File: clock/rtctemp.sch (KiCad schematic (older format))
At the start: 15 parts, among them U601 ADT7410, U602 DS3231, U603 ADT7410

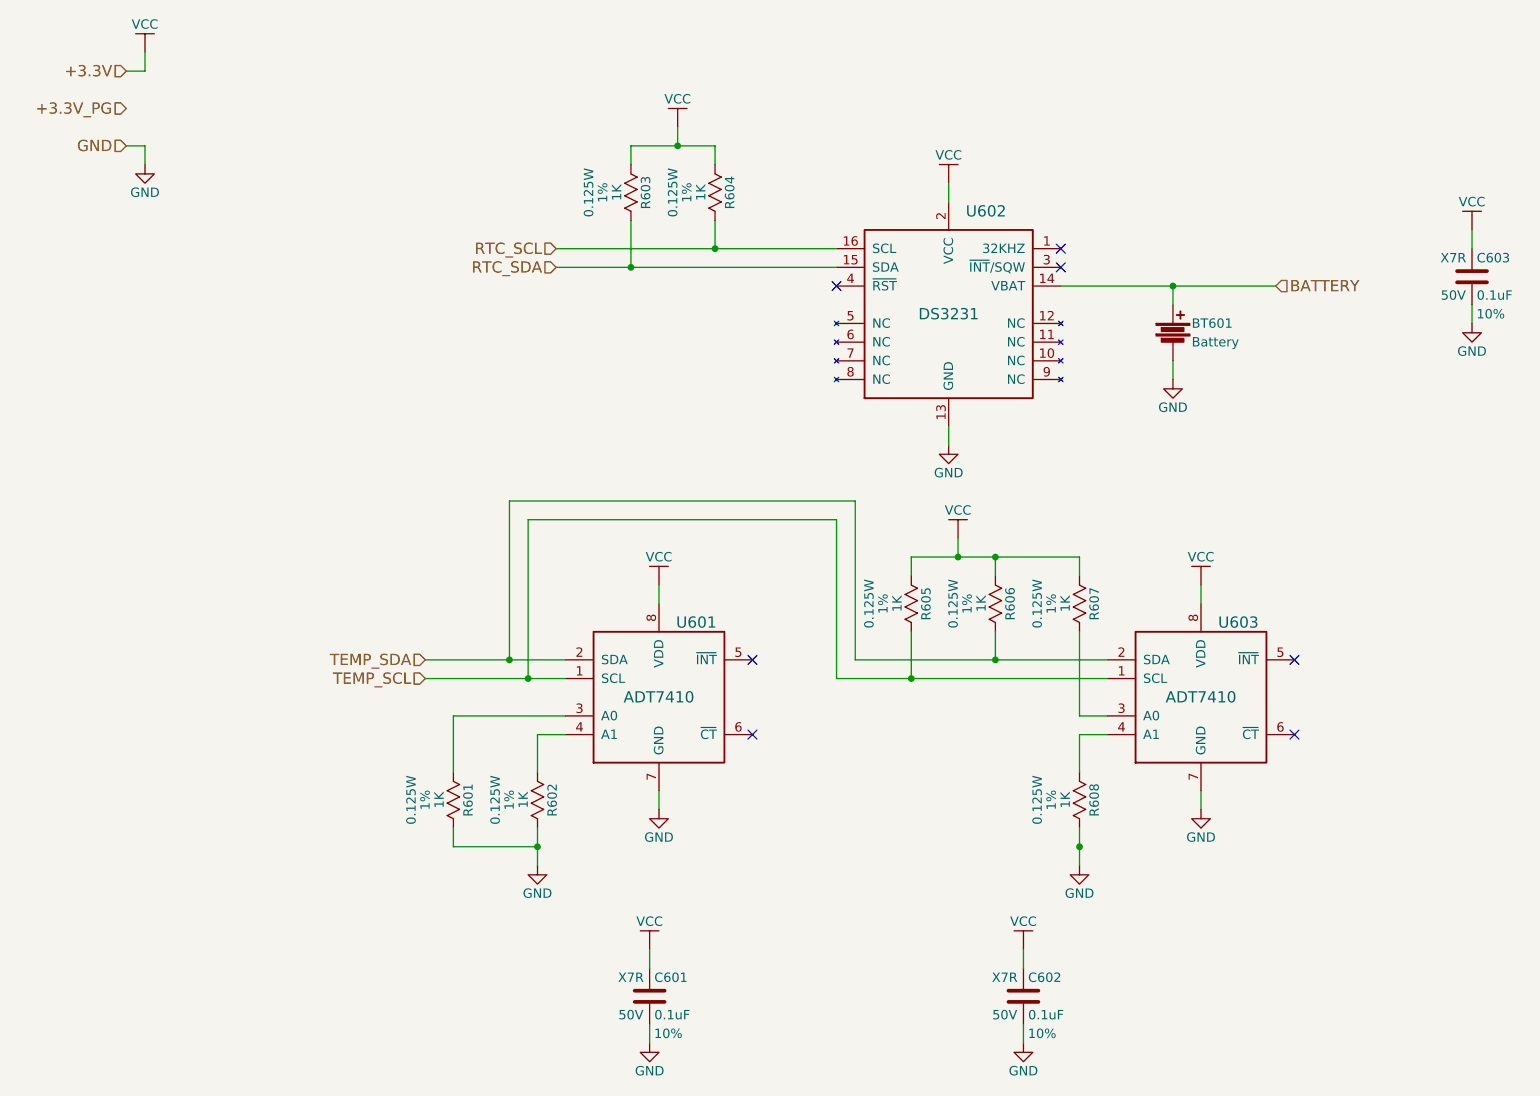
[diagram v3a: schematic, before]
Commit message: Make component parameters consistent for BOM.
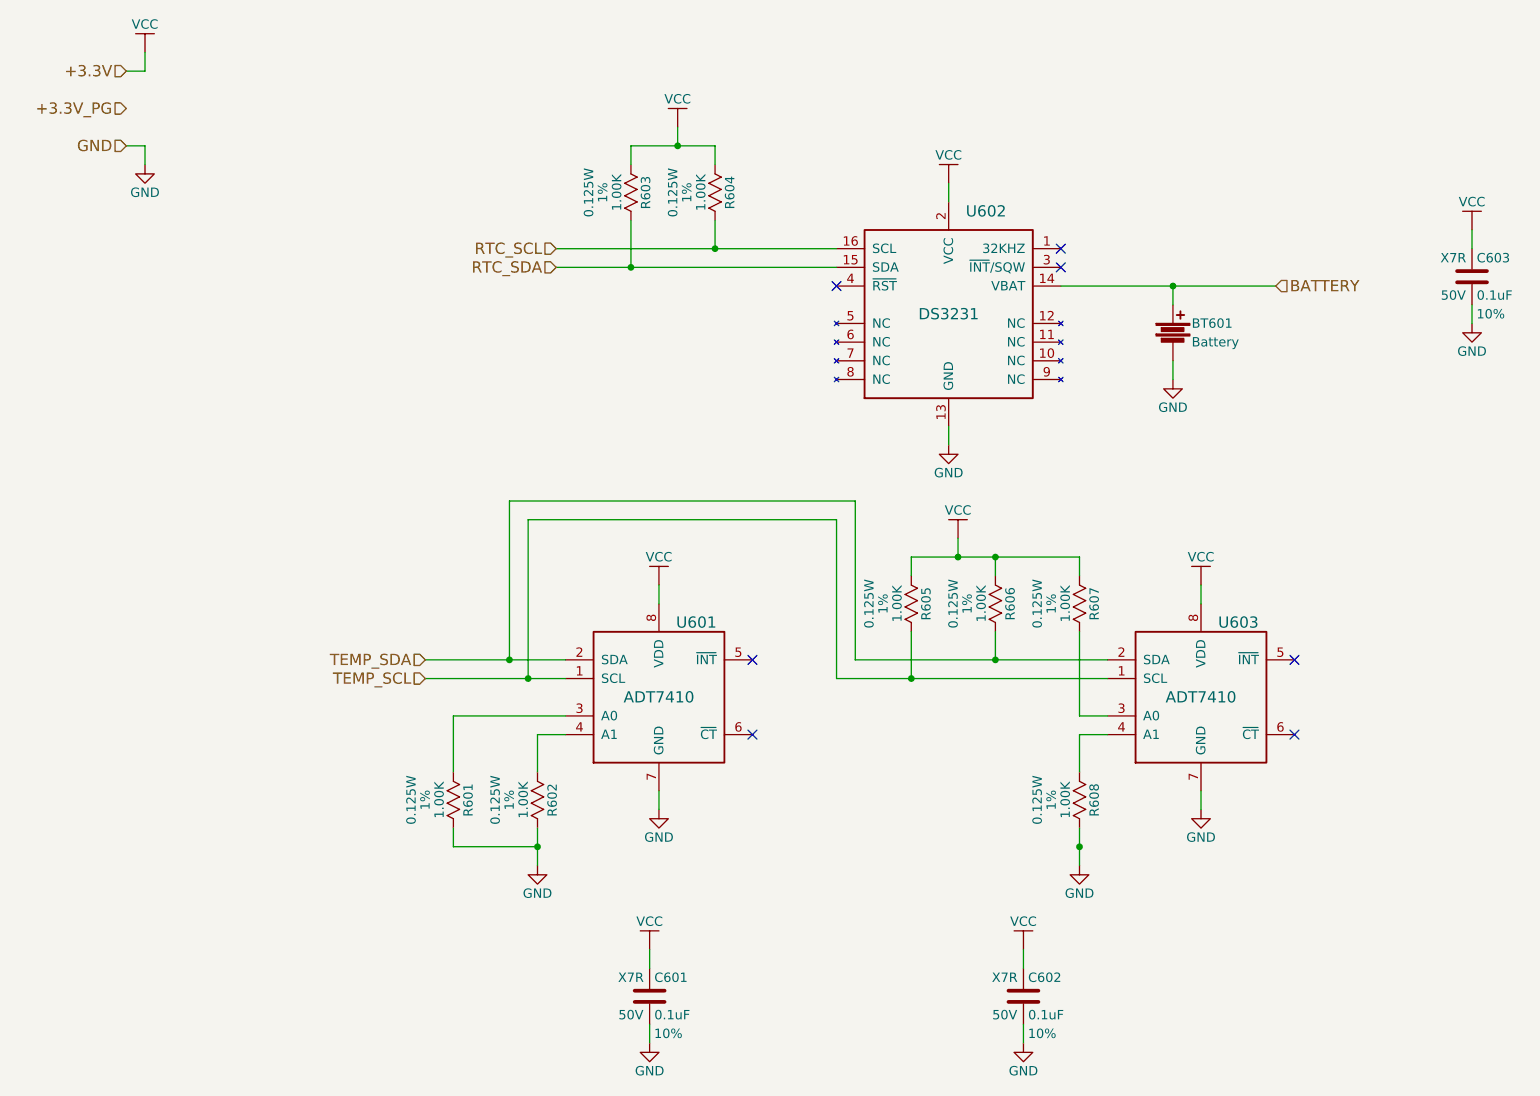
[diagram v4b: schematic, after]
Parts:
- R601, R602, R603, R604, R605, R606, R607, R608: value 1K -> 1.00K
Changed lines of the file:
@@
 P 4050 2050
 F 0 "R603" V 4130 2050 50  0000 C CNN
-F 1 "1K" V 3975 2050 50  0000 C CNN
+F 1 "1.00K" V 3975 2050 50  0000 C CNN
 F 2 "Resistors_SMD:R_0805_HandSoldering" V 3980 2050 30  0001 C CNN
 F 3 "" V 4130 2050 30  0000 C CNN
@@
 P 4500 2050
 F 0 "R604" V 4580 2050 50  0000 C CNN
-F 1 "1K" V 4425 2050 50  0000 C CNN
+F 1 "1.00K" V 4425 2050 50  0000 C CNN
 F 2 "Resistors_SMD:R_0805_HandSoldering" V 4430 2050 30  0001 C CNN
 F 3 "" V 4580 2050 30  0000 C CNN
@@
 P 5550 4250
 F 0 "R605" V 5630 4250 50  0000 C CNN
-F 1 "1K" V 5475 4250 50  0000 C CNN
+F 1 "1.00K" V 5475 4250 50  0000 C CNN
 F 2 "Resistors_SMD:R_0805_HandSoldering" V 5480 4250 30  0001 C CNN
 F 3 "" V 5630 4250 30  0000 C CNN
@@
 P 6000 4250
 F 0 "R606" V 6080 4250 50  0000 C CNN
-F 1 "1K" V 5925 4250 50  0000 C CNN
+F 1 "1.00K" V 5925 4250 50  0000 C CNN
 F 2 "Resistors_SMD:R_0805_HandSoldering" V 5930 4250 30  0001 C CNN
 F 3 "" V 6080 4250 30  0000 C CNN
@@
 P 3100 5300
 F 0 "R601" V 3180 5300 50  0000 C CNN
-F 1 "1K" V 3025 5300 50  0000 C CNN
+F 1 "1.00K" V 3025 5300 50  0000 C CNN
 F 2 "Resistors_SMD:R_0805_HandSoldering" V 3030 5300 30  0001 C CNN
 F 3 "" V 3180 5300 30  0000 C CNN
@@
 P 3550 5300
 F 0 "R602" V 3630 5300 50  0000 C CNN
-F 1 "1K" V 3475 5300 50  0000 C CNN
+F 1 "1.00K" V 3475 5300 50  0000 C CNN
 F 2 "Resistors_SMD:R_0805_HandSoldering" V 3480 5300 30  0001 C CNN
 F 3 "" V 3630 5300 30  0000 C CNN
@@
 P 6450 5300
 F 0 "R608" V 6530 5300 50  0000 C CNN
-F 1 "1K" V 6375 5300 50  0000 C CNN
+F 1 "1.00K" V 6375 5300 50  0000 C CNN
 F 2 "Resistors_SMD:R_0805_HandSoldering" V 6380 5300 30  0001 C CNN
 F 3 "" V 6530 5300 30  0000 C CNN
@@
 P 6450 4250
 F 0 "R607" V 6530 4250 50  0000 C CNN
-F 1 "1K" V 6375 4250 50  0000 C CNN
+F 1 "1.00K" V 6375 4250 50  0000 C CNN
 F 2 "Resistors_SMD:R_0805_HandSoldering" V 6380 4250 30  0001 C CNN
 F 3 "" V 6530 4250 30  0000 C CNN

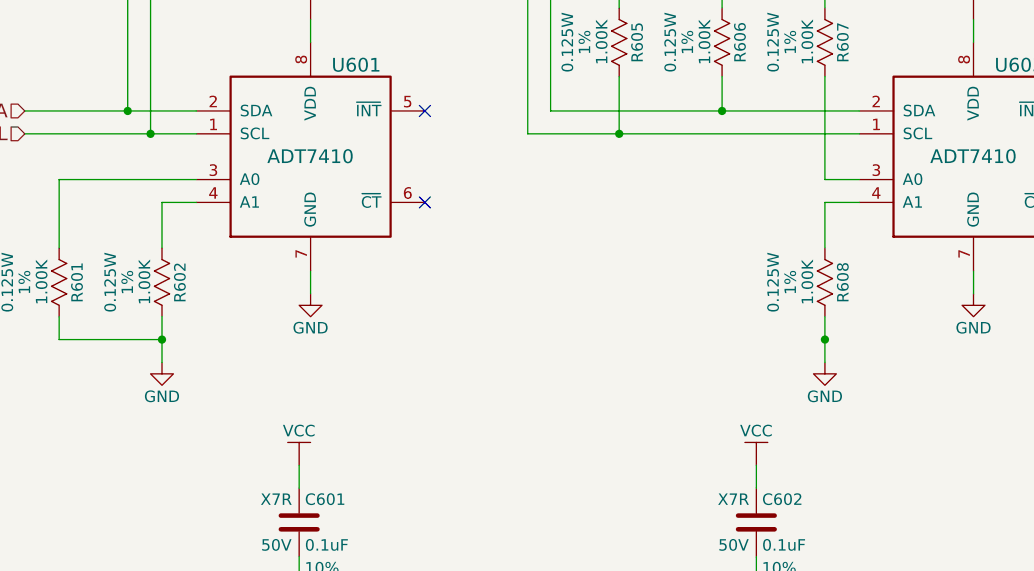
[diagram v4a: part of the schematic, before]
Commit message: Add net names to most of the nets.
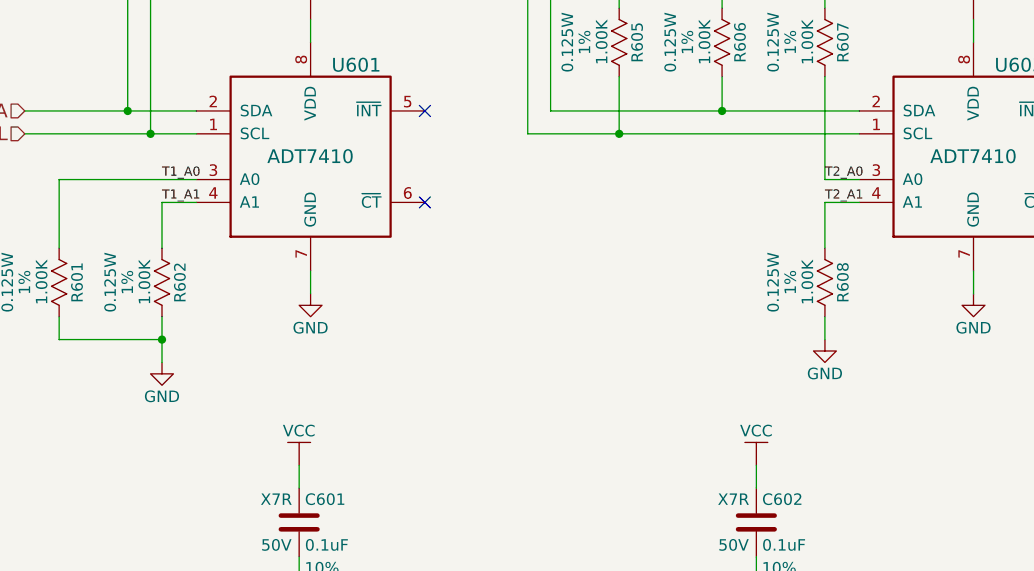
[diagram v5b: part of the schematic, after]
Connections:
- net T1_A0: now reaches R601.1, U601.3 (A0)
- net T1_A1: now reaches R602.1, U601.4 (A1)
- net T2_A0: now reaches R607.2, U603.3 (A0)
- net T2_A1: now reaches R608.1, U603.4 (A1)
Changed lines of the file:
@@
 RTC_SDA
 $Comp
-L GND #PWR076
+L GND #PWR078
 U 1 1 5636B600
 P 1450 1900
-F 0 "#PWR076" H 1450 1650 50  0001 C CNN
+F 0 "#PWR078" H 1450 1650 50  0001 C CNN
 F 1 "GND" H 1450 1750 50  0000 C CNN
 F 2 "" H 1450 1900 60  0000 C CNN
@@
 	5750 3400 5750 3300
 $Comp
-L GND #PWR077
+L GND #PWR079
 U 1 1 5636B6C4
 P 5750 3400
-F 0 "#PWR077" H 5750 3150 50  0001 C CNN
+F 0 "#PWR079" H 5750 3150 50  0001 C CNN
 F 1 "GND" H 5750 3250 50  0000 C CNN
 F 2 "" H 5750 3400 60  0000 C CNN
@@
 $EndComp
 $Comp
-L VCC #PWR078
+L VCC #PWR080
 U 1 1 5636B791
 P 1450 1300
-F 0 "#PWR078" H 1450 1150 50  0001 C CNN
+F 0 "#PWR080" H 1450 1150 50  0001 C CNN
 F 1 "VCC" H 1450 1450 50  0000 C CNN
 F 2 "" H 1450 1300 60  0000 C CNN
@@
 	1450 1400 1450 1300
 $Comp
-L VCC #PWR079
+L VCC #PWR081
 U 1 1 5636B7D2
 P 5750 2000
-F 0 "#PWR079" H 5750 1850 50  0001 C CNN
+F 0 "#PWR081" H 5750 1850 50  0001 C CNN
 F 1 "VCC" H 5750 2150 50  0000 C CNN
 F 2 "" H 5750 2000 60  0000 C CNN
@@
 	4500 1800 4500 1900
 $Comp
-L VCC #PWR080
+L VCC #PWR082
 U 1 1 5636BBAE
 P 4300 1700
-F 0 "#PWR080" H 4300 1550 50  0001 C CNN
+F 0 "#PWR082" H 4300 1550 50  0001 C CNN
 F 1 "VCC" H 4300 1850 50  0000 C CNN
 F 2 "" H 4300 1700 60  0000 C CNN
@@
 	6950 2550 6950 2650
 $Comp
-L GND #PWR081
+L GND #PWR083
 U 1 1 5636BC94
 P 6950 3050
-F 0 "#PWR081" H 6950 2800 50  0001 C CNN
+F 0 "#PWR083" H 6950 2800 50  0001 C CNN
 F 1 "GND" H 6950 2900 50  0000 C CNN
 F 2 "" H 6950 3050 60  0000 C CNN
@@
 $EndComp
 $Comp
-L VCC #PWR082
+L VCC #PWR084
 U 1 1 5636C0D5
 P 4200 4150
-F 0 "#PWR082" H 4200 4000 50  0001 C CNN
+F 0 "#PWR084" H 4200 4000 50  0001 C CNN
 F 1 "VCC" H 4200 4300 50  0000 C CNN
 F 2 "" H 4200 4150 60  0000 C CNN
@@
 	7100 5350 7100 5250
 $Comp
-L GND #PWR083
+L GND #PWR085
 U 1 1 5636C104
 P 7100 5350
-F 0 "#PWR083" H 7100 5100 50  0001 C CNN
+F 0 "#PWR085" H 7100 5100 50  0001 C CNN
 F 1 "GND" H 7100 5200 50  0000 C CNN
 F 2 "" H 7100 5350 60  0000 C CNN
@@
 	4200 5350 4200 5250
 $Comp
-L GND #PWR084
+L GND #PWR086
 U 1 1 5636C11B
 P 4200 5350
-F 0 "#PWR084" H 4200 5100 50  0001 C CNN
+F 0 "#PWR086" H 4200 5100 50  0001 C CNN
 F 1 "GND" H 4200 5200 50  0000 C CNN
 F 2 "" H 4200 5350 60  0000 C CNN
@@
 	6000 4000 6000 4100
 $Comp
-L VCC #PWR085
+L VCC #PWR087
 U 1 1 5636C1AA
 P 5800 3900
-F 0 "#PWR085" H 5800 3750 50  0001 C CNN
+F 0 "#PWR087" H 5800 3750 50  0001 C CNN
 F 1 "VCC" H 5800 4050 50  0000 C CNN
 F 2 "" H 5800 3900 60  0000 C CNN
@@
 Connection ~ 3550 5550
 $Comp
-L GND #PWR086
+L GND #PWR088
 U 1 1 5636C550
 P 3550 5650
-F 0 "#PWR086" H 3550 5400 50  0001 C CNN
+F 0 "#PWR088" H 3550 5400 50  0001 C CNN
 F 1 "GND" H 3550 5500 50  0000 C CNN
 F 2 "" H 3550 5650 60  0000 C CNN
@@
 Wire Wire Line
 	6450 4950 6450 5150
-Wire Wire Line
-	6450 5450 6450 5650
-Connection ~ 6450 5550
-$Comp
-L GND #PWR087
+$Comp
+L GND #PWR089
 U 1 1 5636C5CD
-P 6450 5650
-F 0 "#PWR087" H 6450 5400 50  0001 C CNN
-F 1 "GND" H 6450 5500 50  0000 C CNN
-F 2 "" H 6450 5650 60  0000 C CNN
-F 3 "" H 6450 5650 60  0000 C CNN
-	1    6450 5650
+P 6450 5550
+F 0 "#PWR089" H 6450 5300 50  0001 C CNN
+F 1 "GND" H 6450 5400 50  0000 C CNN
+F 2 "" H 6450 5550 60  0000 C CNN
+F 3 "" H 6450 5550 60  0000 C CNN
+	1    6450 5550
 	1    0    0    -1
 $EndComp
@@
 Connection ~ 3500 4650
 $Comp
-L GND #PWR088
+L GND #PWR090
 U 1 1 5636CF30
 P 8550 2750
-F 0 "#PWR088" H 8550 2500 50  0001 C CNN
+F 0 "#PWR090" H 8550 2500 50  0001 C CNN
 F 1 "GND" H 8550 2600 50  0000 C CNN
 F 2 "" H 8550 2750 60  0000 C CNN
@@
 $EndComp
 $Comp
-L VCC #PWR089
+L VCC #PWR091
 U 1 1 5636D2DE
 P 8550 2250
-F 0 "#PWR089" H 8550 2100 50  0001 C CNN
+F 0 "#PWR091" H 8550 2100 50  0001 C CNN
 F 1 "VCC" H 8550 2400 50  0000 C CNN
 F 2 "" H 8550 2250 60  0000 C CNN
@@
 $EndComp
 $Comp
-L GND #PWR090
+L GND #PWR092
 U 1 1 5636D43C
 P 4150 6600
-F 0 "#PWR090" H 4150 6350 50  0001 C CNN
+F 0 "#PWR092" H 4150 6350 50  0001 C CNN
 F 1 "GND" H 4150 6450 50  0000 C CNN
 F 2 "" H 4150 6600 60  0000 C CNN
@@
 $EndComp
 $Comp
-L VCC #PWR091
+L VCC #PWR093
 U 1 1 5636D44F
 P 4150 6100
-F 0 "#PWR091" H 4150 5950 50  0001 C CNN
+F 0 "#PWR093" H 4150 5950 50  0001 C CNN
 F 1 "VCC" H 4150 6250 50  0000 C CNN
 F 2 "" H 4150 6100 60  0000 C CNN
@@
 $EndComp
 $Comp
-L GND #PWR092
+L GND #PWR094
 U 1 1 5636D49F
 P 6150 6600
-F 0 "#PWR092" H 6150 6350 50  0001 C CNN
+F 0 "#PWR094" H 6150 6350 50  0001 C CNN
 F 1 "GND" H 6150 6450 50  0000 C CNN
 F 2 "" H 6150 6600 60  0000 C CNN
@@
 $EndComp
 $Comp
-L VCC #PWR093
+L VCC #PWR095
 U 1 1 5636D4B2
 P 6150 6100
-F 0 "#PWR093" H 6150 5950 50  0001 C CNN
+F 0 "#PWR095" H 6150 5950 50  0001 C CNN
 F 1 "VCC" H 6150 6250 50  0000 C CNN
 F 2 "" H 6150 6100 60  0000 C CNN
@@
 NoConn ~ 6350 2350
 $Comp
-L VCC #PWR094
+L VCC #PWR096
 U 1 1 563E1DA8
 P 7100 4150
-F 0 "#PWR094" H 7100 4000 50  0001 C CNN
+F 0 "#PWR096" H 7100 4000 50  0001 C CNN
 F 1 "VCC" H 7100 4300 50  0000 C CNN
 F 2 "" H 7100 4150 60  0000 C CNN
@@
 	1    0    0    -1
 $EndComp
+Text Label 3550 4850 0    40   ~ 0
+T1_A0
+Text Label 3550 4950 0    40   ~ 0
+T1_A1
+Text Label 6450 4850 0    40   ~ 0
+T2_A0
+Text Label 6450 4950 0    40   ~ 0
+T2_A1
+Wire Wire Line
+	6450 5550 6450 5450
 $EndSCHEMATC
